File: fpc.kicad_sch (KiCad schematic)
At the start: 0 parts

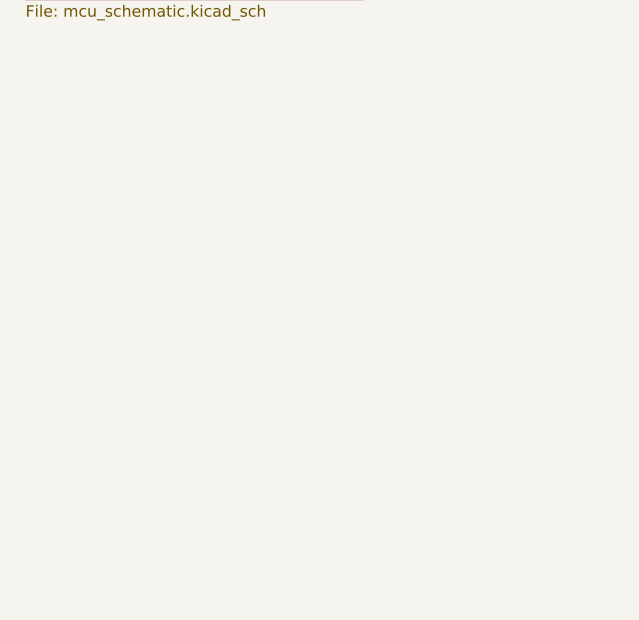
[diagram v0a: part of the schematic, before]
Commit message: add current sensor schematic
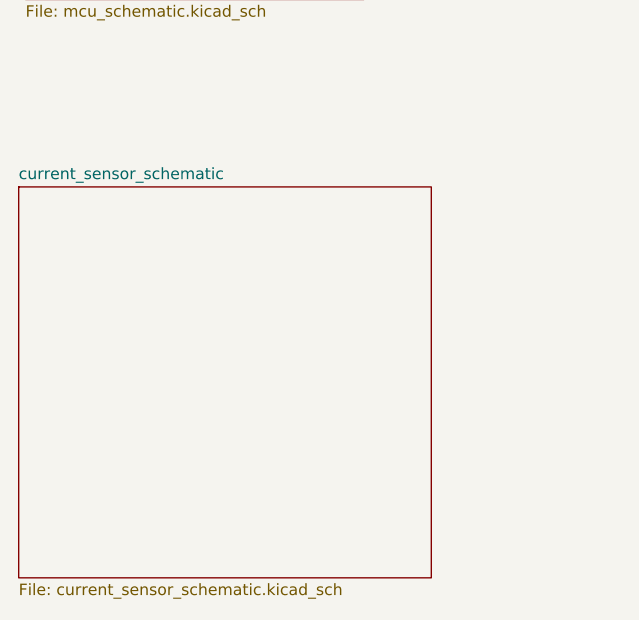
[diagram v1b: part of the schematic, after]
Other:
- added sheet current_sensor_schematic (current_sensor_schematic.kicad_sch)
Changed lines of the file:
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@@
 	(paper "A4")
+	(sheet
+		(at 55.753 149.098)
+		(size 45.847 43.434)
+		(exclude_from_sim no)
+		(in_bom yes)
+		(on_board yes)
+		(dnp no)
+		(fields_autoplaced yes)
+		(stroke
+			(width 0.1524)
+			(type solid)
+		)
+		(fill
+			(color 0 0 0 0.0000)
+		)
+		(property "Sheetname" "current_sensor_schematic"
+			(at 55.753 148.3864 0)
+			(effects
+				(font
+					(size 1.27 1.27)
+				)
+				(justify left bottom)
+			)
+		)
+		(property "Sheetfile" "current_sensor_schematic.kicad_sch"
+			(at 55.753 193.1166 0)
+			(effects
+				(font
+					(size 1.27 1.27)
+				)
+				(justify left top)
+			)
+		)
+		(instances
+			(project "fpc"
+				(path "/01bdb219-e962-46e0-86ef-19b214cb07d2"
+					(page "6")
+				)
+			)
+		)
+	)
 	(sheet
 		(at 130.937 45.466)

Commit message: fpc_hw schematic
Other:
- added sheet fpc_hw (marging.kicad_sch)
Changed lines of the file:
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@@
+	)
+	(sheet
+		(at 111.76 96.52)
+		(size 91.44 60.96)
+		(exclude_from_sim no)
+		(in_bom yes)
+		(on_board yes)
+		(dnp no)
+		(fields_autoplaced yes)
+		(stroke
+			(width 0.1524)
+			(type solid)
+		)
+		(fill
+			(color 0 0 0 0.0000)
+		)
+		(property "Sheetname" "fpc_hw"
+			(at 111.76 95.8084 0)
+			(effects
+				(font
+					(size 1.27 1.27)
+				)
+				(justify left bottom)
+			)
+		)
+		(property "Sheetfile" "marging.kicad_sch"
+			(at 111.76 158.0646 0)
+			(effects
+				(font
+					(size 1.27 1.27)
+				)
+				(justify left top)
+			)
+		)
+		(instances
+			(project "fpc"
+				(path "/01bdb219-e962-46e0-86ef-19b214cb07d2"
+					(page "7")
+				)
+			)
+		)
 	)
 	(sheet

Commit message: new update of schematic and pcb
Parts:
- added H1, H2, H3, H4, H5, H6, H7, H8: MountingHole_Pad, MountingHole:MountingHole_3.2mm_M3_DIN965_Pad, symbol Mechanical:MountingHole_Pad
- added IN1, IN6, IN7, IN8: D, Diode_THT:D_DO-41_SOD81_P10.16mm_Horizontal, symbol Device:D
- added J1, J2: Conn_01x15_Socket, Connector_PinHeader_2.54mm:PinHeader_1x15_P2.54mm_Vertical, symbol Connector:Conn_01x15_Socket
- added J16, J17, J18, J19, J20, J21, J3, J4: Screw_Terminal_01x04, TerminalBlock_Phoenix:TerminalBlock_Phoenix_MPT-0,5-4-2.54_1x04_P2.54mm_Horizontal, symbol Connector:Screw_Terminal_01x04
- added J22: 15v, TerminalBlock:TerminalBlock_MaiXu_MX126-5.0-02P_1x02_P5.00mm, symbol Connector:Screw_Terminal_01x02
- added J5: Conn_01x02_Socket, Connector_PinHeader_2.54mm:PinHeader_1x02_P2.54mm_Vertical, symbol Connector:Conn_01x02_Socket
- added K1, K6, K7, K8: G2RL-2, Relay_THT:Relay_DPDT_Omron_G2RL-2, symbol Relay:G2RL-2
- added Q1, Q6, Q7, Q8: BC547, Package_TO_SOT_THT:TO-92_Inline, symbol Transistor_BJT:BC547
- added R1, R2, R3, R4: 1k, Resistor_THT:R_Axial_DIN0207_L6.3mm_D2.5mm_P7.62mm_Horizontal, symbol Device:R_US
- added U1, U2, U3, U4: ~, Custom:ACS712_Current_Sensor, symbol ASC712_current_sensor:ASC712_Current_sensor
- added U10: ~, LM259_THT:LM2596, symbol New_Library:LM2596
- added U5: DEVKIT_V1_ESP32-WROOM-32, Custom:MODULE_ESP32-DEVKITC-32E, symbol DEVKIT_V1_ESP32-WROOM-32:DEVKIT_V1_ESP32-WROOM-32
- added U6: RS485_TTL_Module, Custom:MODULE_MAX485_MODULE_5V_LOGIC_TLL_TO_RS-485_CONVERTER, symbol rs485_ttl_sym:rs485_ttl_sm
- added U7: ZC261500, Custom:MODULE_ZC261500, symbol ADS1115_module:ZC261500
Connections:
- new net: Q6.2 (B), R1.2
- new net: IN6.2 (A), K6.A2, Q6.1 (C)
- new net: IN8.2 (A), K8.A2, Q8.1 (C)
- new net: Q8.2 (B), R4.2
- new net: U6.2 (RE), U6.3 (DE)
- new net: U5.33 (IO21), U7.7 (SDA)
- new net: U5.36 (IO22), U7.8 (SCL)
- new net: IN1.2 (A), K1.A2, Q1.1 (C)
- new net: Q1.2 (B), R3.2
- new net: Q7.2 (B), R2.2
- new net: IN7.2 (A), K7.A2, Q7.1 (C)
- new net: J22.1 (Pin_1), U10.1 (IN+)
- new net: J22.2 (Pin_2), U10.2 (IN-)
- new net +3.3V: J1.9 (Pin_9), U6.8 (VCC)
- new net +5V: J2.14 (Pin_14), U10.3 (OUT+), U7.10 (VDD)
- new net -1PUMP+: K7.14, U1.5 (IP_-(I_Out))
- new net -2PUMP+: K8.14, U3.5 (IP_-(I_Out))
- new net -3PUMP+: K6.14, U2.5 (IP_-(I_Out))
- new net -4PUMP+: K1.14, U4.5 (IP_-(I_Out))
- new net 1AC+: J18.4 (Pin_4), K7.11
- new net 1AC-: J18.3 (Pin_3), K7.21
- new net 1PUMP+: J18.1 (Pin_1), U1.6 (IP+(I_in))
- new net 1PUMP-: J18.2 (Pin_2), K7.24
- new net 2: J16.2 (Pin_2), J17.2 (Pin_2), J3.2 (Pin_2), J4.2 (Pin_2), U6.7 (B)
- new net 2AC+: J19.4 (Pin_4), K8.11
- new net 2AC-: J19.3 (Pin_3), K8.21
- new net 2PUMP+: J19.1 (Pin_1), U3.6 (IP+(I_in))
- new net 2PUMP-: J19.2 (Pin_2), K8.24
- new net 3: J16.3 (Pin_3), J17.3 (Pin_3), J3.3 (Pin_3), J4.3 (Pin_3), U6.6 (A)
- new net 3.3V: J2.9 (Pin_9), U5.1 (3V3)
- new net 3AC+: J20.4 (Pin_4), K6.11
- new net 3AC-: J20.3 (Pin_3), K6.21
- new net 3PUMP+: J20.1 (Pin_1), U2.6 (IP+(I_in))
- new net 3PUMP-: J20.2 (Pin_2), K6.24
- new net 4AC+: J21.4 (Pin_4), K1.11
- new net 4AC-: J21.3 (Pin_3), K1.21
- new net 4PUMP+: J21.1 (Pin_1), U4.6 (IP+(I_in))
- new net 4PUMP-: J21.2 (Pin_2), K1.24
- new net A0: J1.4 (Pin_4), U1.2 (OUT)
- new net A0+: J2.4 (Pin_4), U7.4 (A0)
- new net A1: J1.8 (Pin_8), U3.2 (OUT)
- new net A1+: J2.8 (Pin_8), U7.3 (A1)
- new net A2: J1.2 (Pin_2), U2.2 (OUT)
- new net A2+: J2.2 (Pin_2), U7.2 (A2)
- new net A3: J1.6 (Pin_6), U4.2 (OUT)
- new net A3+: J2.6 (Pin_6), U7.1 (A3)
- new net D1: J1.10 (Pin_10), U6.4 (DI)
- new net D1+: J2.10 (Pin_10), U5.28 (IO17)
- new net GND: H1.1, H2.1, H3.1, H4.1, H5.1, H6.1, H7.1, H8.1, J1.15 (Pin_15), J16.4 (Pin_4), J17.4 (Pin_4), J2.15 (Pin_15), J3.4 (Pin_4), J4.4 (Pin_4), J5.2 (Pin_2), Q1.3 (E), Q6.3 (E), Q7.3 (E), Q8.3 (E), U1.1 (GND), U10.4 (OUT-), U2.1 (GND), U3.1 (GND), U4.1 (GND), U6.5 (GND), U7.6 (ADDR), U7.9 (GND)
- new net GPIO14: J2.7 (Pin_7), U5.12 (IO14)
- new net GPIO25: J2.1 (Pin_1), U5.9 (IO25)
- new net GPIO26: J2.3 (Pin_3), U5.10 (IO26)
- new net GPIO27: J2.5 (Pin_5), U5.11 (IO27)
- new net GPIO4: J5.1 (Pin_1), U5.26 (IO4)
- new net R0: J1.11 (Pin_11), U6.1 (R0)
- new net R0+: J2.11 (Pin_11), U5.27 (IO16)
- new net R1: J1.1 (Pin_1), R1.1
- new net R2: J1.3 (Pin_3), R2.1
- new net R3: J1.5 (Pin_5), R3.1
- new net R4: J1.7 (Pin_7), R4.1
- new net VCC: IN1.1 (K), IN6.1 (K), IN7.1 (K), IN8.1 (K), J1.14 (Pin_14), J16.1 (Pin_1), J17.1 (Pin_1), J3.1 (Pin_1), J4.1 (Pin_1), K1.A1, K6.A1, K7.A1, K8.A1, U1.3 (VCC), U2.3 (VCC), U3.3 (VCC), U4.3 (VCC)
- no-connect marks 0 -> 41
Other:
- removed sheet current_sensor_schematic
- removed sheet fpc_hw
- removed sheet level_sensor
- removed sheet mcu_schematic
- removed sheet power_schematic
- removed sheet relay_schematic

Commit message: latest update
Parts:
- removed J1, J2: Conn_01x15_Socket, Connector_PinHeader_2.54mm:PinHeader_1x15_P2.54mm_Vertical, symbol Connector:Conn_01x15_Socket
- removed K1, K6, K7, K8: G2RL-2, Relay_THT:Relay_DPDT_Omron_G2RL-2, symbol Relay:G2RL-2
- added J6, J7: Conn_01x16_Socket, Connector_PinHeader_2.54mm:PinHeader_1x16_P2.54mm_Vertical, symbol Connector:Conn_01x16_Socket
- added K1, K2, K3, K4: Relay_SPDT, Relay_THT:Relay_SPDT_SANYOU_SRD_Series_Form_C, symbol Relay:Relay_SPDT
- added SW1: SW_Push, symbol Switch:SW_Push
- J16, J17, J18, J19, J20, J21, J3, J4: footprint TerminalBlock_Phoenix:TerminalBlock_Phoenix_MPT-0,5-4-2.54_1x04_P2.54mm_Horizontal -> TerminalBlock_Phoenix:TerminalBlock_Phoenix_PT-1,5-4-5.0-H_1x04_P5.00mm_Horizontal
- U5: footprint Custom:MODULE_ESP32-DEVKITC-32E -> custom:MODULE_ESP32_NODEMCU
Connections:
- net 1PUMP- is gone; now on an unnamed net: J18.2 (Pin_2)
- net 2PUMP- is gone; now on an unnamed net: J19.2 (Pin_2)
- net 3PUMP- is gone; now on an unnamed net: J20.2 (Pin_2)
- net 4PUMP- is gone; now on an unnamed net: J21.2 (Pin_2)
- net +3.3V: now also J7.9 (Pin_9)
- net +5V: now also U5.19 (EXT_5V), J6.15 (Pin_15)
- net -1PUMP+: now also K2.3
- net -2PUMP+: now also K4.3
- net -3PUMP+: now also K1.3
- net -4PUMP+: now also K3.3
- net 1AC+: now also K2.1
- net 3.3V: now also J6.9 (Pin_9)
- net 3AC+: now also K1.1
- net 4AC+: now also K3.1
- net A0: now also J7.4 (Pin_4)
- net A0+: now also J6.4 (Pin_4)
- net A1: now also J7.8 (Pin_8)
- net A1+: now also J6.8 (Pin_8)
- net A2: now also J7.2 (Pin_2)
- net A2+: now also J6.2 (Pin_2)
- net A3: now also J7.6 (Pin_6)
- net A3+: now also J6.6 (Pin_6)
- net D1: now also J7.10 (Pin_10)
- net D1+: now also J6.10 (Pin_10)
- net GND: now also U5.32 (GND2), U5.38 (GND3), J6.16 (Pin_16), J7.16 (Pin_16)
- net GPIO14: now also J6.7 (Pin_7)
- net GPIO25: now also J6.1 (Pin_1)
- net GPIO26: now also J6.3 (Pin_3)
- net GPIO27: now also J6.5 (Pin_5)
- net R0: now also J7.11 (Pin_11)
- net R0+: now also J6.11 (Pin_11)
- net R1: now also J7.1 (Pin_1)
- net R2: now also J7.3 (Pin_3)
- net R3: now also J7.5 (Pin_5)
- net R4: now also J7.7 (Pin_7)
- net VCC: now also J7.15 (Pin_15), K1.5, K2.5, K3.5, K4.5
- net at IN6.2 (A), Q6.1 (C): now also K1.2
- net at IN8.2 (A), Q8.1 (C): now also K4.2
- net RE: now reaches U6.2 (RE), U6.3 (DE)
- net RE: now also J7.12 (Pin_12)
- net at IN1.2 (A), Q1.1 (C): now also K3.2
- net at IN7.2 (A), Q7.1 (C): now also K2.2
- net RE+: now reaches U5.29 (IO5)
- net RE+: now also J6.12 (Pin_12)
- net 1AC-: no longer names the net of J18.3 (Pin_3)
- net 2AC-: no longer names the net of J19.3 (Pin_3)
- net 3AC-: no longer names the net of J20.3 (Pin_3)
- net 4AC-: no longer names the net of J21.3 (Pin_3)
- no-connect marks 41 -> 34
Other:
- note added: "(FPC-HW PROJECT)"
- note added: "WATER PUMPING MACHINE AUTOMATIC SWITCH"
- moved on the sheet: IN1, IN6, IN7, IN8, J18, J19, J20, J21, J22, J5, Q1, Q6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
